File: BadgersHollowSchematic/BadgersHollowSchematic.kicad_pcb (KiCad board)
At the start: 2 copper layers, 33 x 48.3 mm, 5 parts

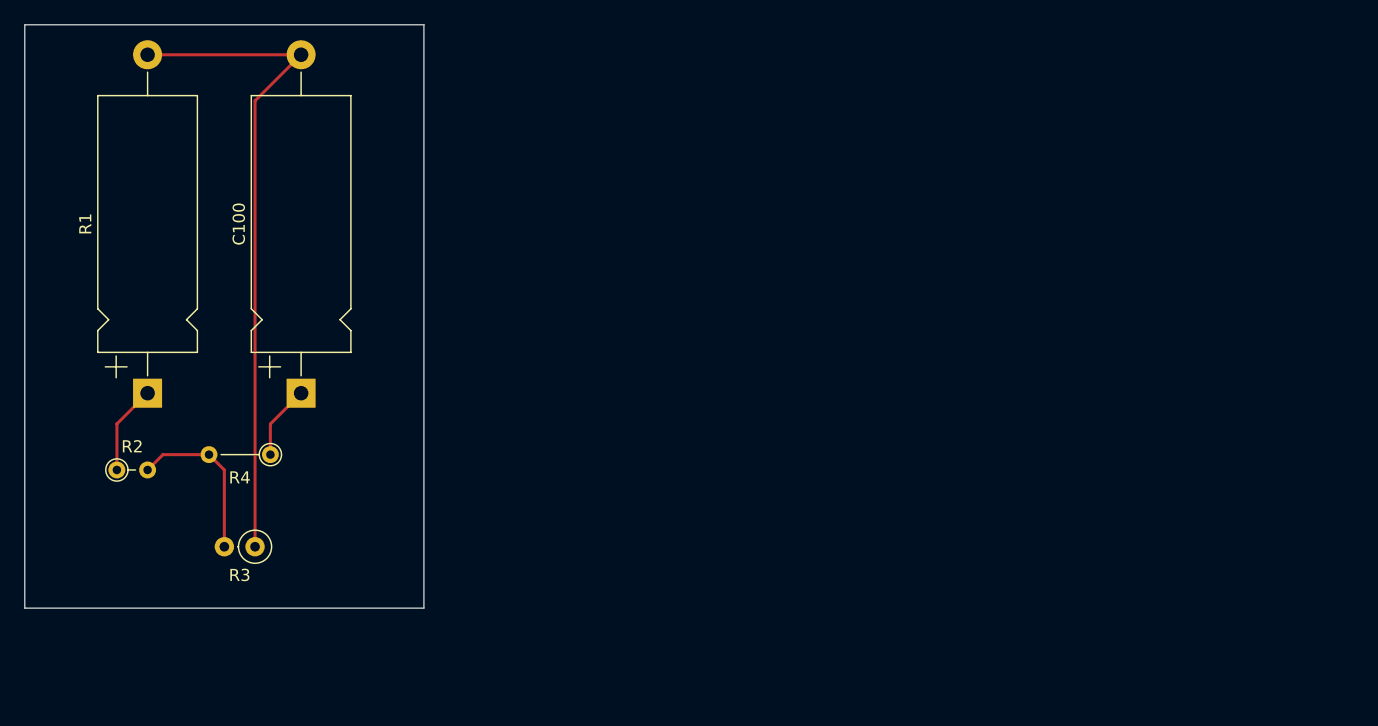
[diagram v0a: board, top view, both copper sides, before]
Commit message: Schematic down. Need to review, and map columns/rows to correct pins
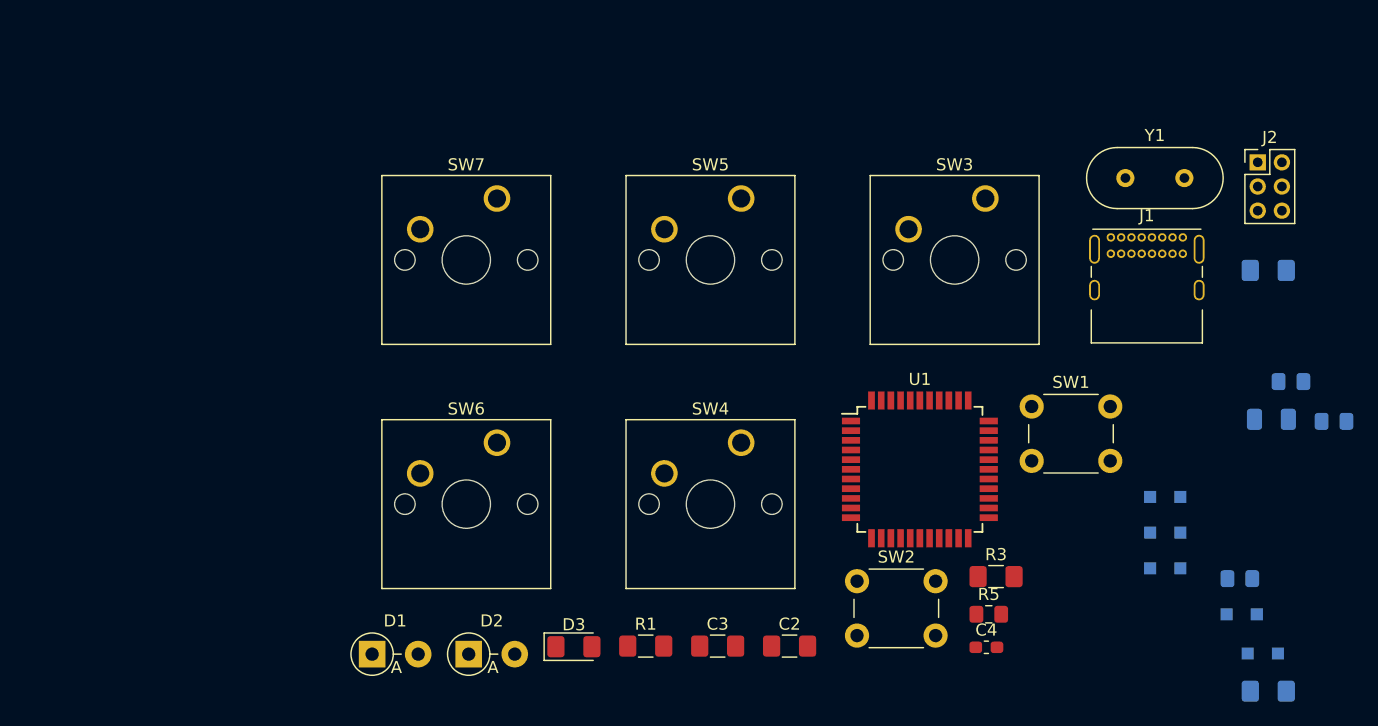
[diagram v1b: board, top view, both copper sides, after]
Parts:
- removed C100: 10, Capacitor_THT:CP_Axial_L21.0mm_D8.0mm_P28.00mm_Horizontal
- added C1: 22pF, Capacitor_SMD:C_1206_3216Metric_Pad1.42x1.75mm_HandSolder, B.Cu at (207.0, 71.1)
- added C2: 22pF, Capacitor_SMD:C_1206_3216Metric_Pad1.42x1.75mm_HandSolder, F.Cu at (167.4, 102.2)
- added C3: 1uF, Resistor_SMD:R_1206_3216Metric_Pad1.42x1.75mm_HandSolder, F.Cu at (161.5, 102.2)
- added C4: 10uF, Capacitor_SMD:C_0603_1608Metric_Pad1.05x0.95mm_HandSolder, F.Cu at (183.7, 102.3)
- added D1: 3.6V, Diode_THT:D_DO-41_SOD81_P3.81mm_Vertical_AnodeUp, F.Cu at (132.9, 102.9)
- added D2: 3.6V, Diode_THT:D_DO-41_SOD81_P3.81mm_Vertical_AnodeUp, F.Cu at (140.9, 102.9)
- added D3: LED, LED_SMD:LED_1206_3216Metric_Pad1.42x1.75mm_HandSolder, F.Cu at (149.6, 102.2)
- added D4: 1N4148, Diode_SMD:D_SOD-323_HandSoldering, B.Cu at (204.8, 99.6)
- added D5: 1N4148, Diode_SMD:D_SOD-323_HandSoldering, B.Cu at (198.5, 89.9)
- added D6: 1N4148, Diode_SMD:D_SOD-323_HandSoldering, B.Cu at (198.5, 92.8)
- added D7: 1N4148, Diode_SMD:D_SOD-323_HandSoldering, B.Cu at (206.6, 102.8)
- added D8: 1N4148, Diode_SMD:D_SOD-323_HandSoldering, B.Cu at (198.5, 95.8)
- added F1: Polyfuse_Small, Fuse:Fuse_1206_3216Metric, B.Cu at (207.3, 83.4)
- added J1: usbc_gct, Connector_USB:USB_C_Receptacle_GCT_USB4085, F.Cu at (194.0, 68.4)
- added J2: AVR-ISP-6, Connector_PinHeader_2.00mm:PinHeader_2x03_P2.00mm_Vertical, F.Cu at (206.1, 62.2)
- added R5: 22, Resistor_SMD:R_0805_2012Metric_Pad1.15x1.40mm_HandSolder, F.Cu at (183.9, 99.6)
- added R6: 1.5K, Resistor_SMD:R_0805_2012Metric_Pad1.15x1.40mm_HandSolder, B.Cu at (208.9, 80.3)
- added R7: 1.5K, Resistor_SMD:R_0805_2012Metric_Pad1.15x1.40mm_HandSolder, B.Cu at (204.7, 96.6)
- added SW1: SW_Push, Button_Switch_THT:SW_PUSH_6mm, F.Cu at (187.4, 82.4)
- added SW2: SW_Push, Button_Switch_THT:SW_PUSH_6mm, F.Cu at (173.0, 96.8)
- added SW3: SW_SPST, Button_Switch_Keyboard:SW_Cherry_MX_1.00u_PCB, F.Cu at (183.6, 65.2)
- added SW4: SW_SPST, Button_Switch_Keyboard:SW_Cherry_MX_1.00u_PCB, F.Cu at (163.4, 85.4)
- added SW5: SW_SPST, Button_Switch_Keyboard:SW_Cherry_MX_1.00u_PCB, F.Cu at (163.4, 65.2)
- added SW6: SW_SPST, Button_Switch_Keyboard:SW_Cherry_MX_1.00u_PCB, F.Cu at (143.2, 85.4)
- added SW7: SW_SPST, Button_Switch_Keyboard:SW_Cherry_MX_1.00u_PCB, F.Cu at (143.2, 65.2)
- added U1: ATmega32U4-AU, Package_QFP:TQFP-44_10x10mm_P0.8mm, F.Cu at (178.2, 87.6)
- added Y1: Crystal, Crystal:Crystal_HC49-U_Vertical, F.Cu at (195.2, 63.5)
- R1: value 100 -> 10K; footprint Capacitor_THT:CP_Axial_L21.0mm_D8.0mm_P28.00mm_Horizontal -> Resistor_SMD:R_1206_3216Metric_Pad1.42x1.75mm_HandSolder
- R2: value 200 -> 5.1K; footprint Resistor_THT:R_Axial_DIN0204_L3.6mm_D1.6mm_P2.54mm_Vertical -> Resistor_SMD:R_1206_3216Metric_Pad1.42x1.75mm_HandSolder; moved to B.Cu
- R3: value 300 -> 5.1K; footprint Resistor_THT:R_Axial_DIN0207_L6.3mm_D2.5mm_P2.54mm_Vertical -> Resistor_SMD:R_1206_3216Metric_Pad1.42x1.75mm_HandSolder
- R4: value 400 -> 22; footprint Resistor_THT:R_Axial_DIN0204_L3.6mm_D1.6mm_P5.08mm_Vertical -> Resistor_SMD:R_0805_2012Metric_Pad1.15x1.40mm_HandSolder; moved to B.Cu
- moved R2 97.0 mm to (207.0, 105.9)
- moved R4 88.0 mm to (212.4, 83.6), turned to 0 degrees
- moved R3 61.3 mm to (184.5, 96.5), turned to 0 degrees
- moved R1 46.2 mm to (155.5, 102.2), turned to 0 degrees
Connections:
- R1 pad 1: Net-(R1-Pad1) -> +5V
- R1 pad 2: Net-(C100-Pad2) -> Reset
- R2 pad 1: Net-(R1-Pad1) -> GND
- R2 pad 2: GND -> Net-(J1-PadA5)
- R3 pad 1: Net-(C100-Pad2) -> GND
- R3 pad 2: GND -> Net-(J1-PadB5)
- R4 pad 1: Net-(C100-Pad1) -> d-
- R4 pad 2: GND -> Net-(D1-Pad1)
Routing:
- net Net-(C100-Pad2): track 55.0 -> 0.00 mm
- net GND: track 13.8 -> 0.00 mm
- net Net-(R1-Pad1): track 7.40 -> 0.00 mm
- net Net-(C100-Pad1): track 6.13 -> 0.00 mm
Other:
- board outline removed

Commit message: Working on layout
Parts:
- added C10: 0.1uF, Capacitor_SMD:C_0805_2012Metric_Pad1.15x1.40mm_HandSolder, B.Cu at (230.5, 64.8)
- added C11: 0.1uF, Capacitor_SMD:C_0805_2012Metric_Pad1.15x1.40mm_HandSolder, B.Cu at (241.3, 73.7)
- added C12: 0.1uF, Capacitor_SMD:C_0805_2012Metric_Pad1.15x1.40mm_HandSolder, B.Cu at (241.3, 68.6)
- added C13: 0.1uF, Capacitor_SMD:C_0805_2012Metric_Pad1.15x1.40mm_HandSolder, B.Cu at (227.1, 57.8)
- added C14: 0.1uF, Capacitor_SMD:C_0805_2012Metric_Pad1.15x1.40mm_HandSolder, B.Cu at (233.0, 59.1)
- added C15: 0.1uF, Capacitor_SMD:C_0805_2012Metric_Pad1.15x1.40mm_HandSolder, B.Cu at (204.5, 81.3)
- added C16: 0.1uF, Capacitor_SMD:C_0805_2012Metric_Pad1.15x1.40mm_HandSolder, B.Cu at (233.3, 73.7)
- added C17: 0.1uF, Capacitor_SMD:C_0805_2012Metric_Pad1.15x1.40mm_HandSolder, B.Cu at (237.5, 78.7)
- added C18: 0.1uF, Capacitor_SMD:C_0805_2012Metric_Pad1.15x1.40mm_HandSolder, B.Cu at (203.2, 74.9)
- added C19: 0.1uF, Capacitor_SMD:C_0805_2012Metric_Pad1.15x1.40mm_HandSolder, B.Cu at (224.3, 78.1)
- added C20: 0.1uF, Capacitor_SMD:C_0805_2012Metric_Pad1.15x1.40mm_HandSolder, B.Cu at (224.5, 65.9)
- added C21: 0.1uF, Capacitor_SMD:C_0805_2012Metric_Pad1.15x1.40mm_HandSolder, B.Cu at (201.8, 69.1)
- added C22: 0.1uF, Capacitor_SMD:C_0805_2012Metric_Pad1.15x1.40mm_HandSolder, B.Cu at (227.0, 68.9)
- added C23: 0.1uF, Capacitor_SMD:C_0805_2012Metric_Pad1.15x1.40mm_HandSolder, B.Cu at (218.2, 72.6)
- added C24: 0.1uF, Capacitor_SMD:C_0805_2012Metric_Pad1.15x1.40mm_HandSolder, B.Cu at (216.0, 61.4)
- added C25: 0.1uF, Capacitor_SMD:C_0805_2012Metric_Pad1.15x1.40mm_HandSolder, B.Cu at (206.8, 69.5)
- added C26: 0.1uF, Capacitor_SMD:C_0805_2012Metric_Pad1.15x1.40mm_HandSolder, B.Cu at (212.7, 73.7)
- added C27: 0.1uF, Capacitor_SMD:C_0805_2012Metric_Pad1.15x1.40mm_HandSolder, B.Cu at (216.5, 78.7)
- added C28: 0.1uF, Capacitor_SMD:C_0805_2012Metric_Pad1.15x1.40mm_HandSolder, B.Cu at (221.0, 61.8)
- added C5: 0.1uF, Capacitor_SMD:C_0805_2012Metric_Pad1.15x1.40mm_HandSolder, B.Cu at (231.8, 68.9)
- added C6: 0.1uF, Capacitor_SMD:C_0805_2012Metric_Pad1.15x1.40mm_HandSolder, B.Cu at (226.1, 73.0)
- added C7: 0.1uF, Capacitor_SMD:C_0805_2012Metric_Pad1.15x1.40mm_HandSolder, B.Cu at (218.2, 69.6)
- added C8: 0.1uF, Capacitor_SMD:C_0805_2012Metric_Pad1.15x1.40mm_HandSolder, B.Cu at (229.1, 78.1)
- added C9: 0.1uF, Capacitor_SMD:C_0805_2012Metric_Pad1.15x1.40mm_HandSolder, B.Cu at (234.9, 63.5)
- added D10: 1N4148, Diode_SMD:D_SOD-323_HandSoldering, F.Cu at (244.8, 105.2)
- added D11: 1N4148, Diode_SMD:D_SOD-323_HandSoldering, F.Cu at (219.7, 130.0)
- added D12: 1N4148, Diode_SMD:D_SOD-323_HandSoldering, F.Cu at (262.8, 109.2)
- added D13: 1N4148, Diode_SMD:D_SOD-323_HandSoldering, F.Cu at (247.3, 101.9)
- added D14: 1N4148, Diode_SMD:D_SOD-323_HandSoldering, F.Cu at (278.8, 94.0)
- added D15: 1N4148, Diode_SMD:D_SOD-323_HandSoldering, F.Cu at (273.7, 94.0)
- added D16: 1N4148, Diode_SMD:D_SOD-323_HandSoldering, F.Cu at (253.5, 114.6)
- added D18: 1N4148, Diode_SMD:D_SOD-323_HandSoldering, F.Cu at (250.1, 121.2)
- added D19: 1N4148, Diode_SMD:D_SOD-323_HandSoldering, F.Cu at (238.9, 111.4)
- added D20: 1N4148, Diode_SMD:D_SOD-323_HandSoldering, F.Cu at (238.9, 108.5)
- added D21: 1N4148, Diode_SMD:D_SOD-323_HandSoldering, F.Cu at (242.6, 127.8)
- added D22: 1N4148, Diode_SMD:D_SOD-323_HandSoldering, F.Cu at (273.7, 97.0)
- added D23: 1N4148, Diode_SMD:D_SOD-323_HandSoldering, F.Cu at (265.3, 105.5)
- added D24: 1N4148, Diode_SMD:D_SOD-323_HandSoldering, F.Cu at (245.1, 124.2)
- added D25: 1N4148, Diode_SMD:D_SOD-323_HandSoldering, F.Cu at (253.5, 117.5)
- added D26: 1N4148, Diode_SMD:D_SOD-323_HandSoldering, F.Cu at (230.4, 118.4)
- added D27: 1N4148, Diode_SMD:D_SOD-323_HandSoldering, F.Cu at (249.7, 86.4)
- added D28: 1N4148, Diode_SMD:D_SOD-323_HandSoldering, F.Cu at (265.3, 102.6)
- added D29: SK6812, LED_SMD:LED_SK6812_PLCC4_5.0x5.0mm_P3.2mm, B.Cu at (194.1, 36.3)
- added D30: SK6812, LED_SMD:LED_SK6812_PLCC4_5.0x5.0mm_P3.2mm, B.Cu at (181.5, 19.8)
- added D31: SK6812, LED_SMD:LED_SK6812_PLCC4_5.0x5.0mm_P3.2mm, B.Cu at (189.9, 26.4)
- added D32: SK6812, LED_SMD:LED_SK6812_PLCC4_5.0x5.0mm_P3.2mm, B.Cu at (212.1, 41.9)
- added D33: SK6812, LED_SMD:LED_SK6812_PLCC4_5.0x5.0mm_P3.2mm, B.Cu at (222.4, 50.4)
- added D34: SK6812, LED_SMD:LED_SK6812_PLCC4_5.0x5.0mm_P3.2mm, B.Cu at (230.8, 43.8)
- added D35: SK6812, LED_SMD:LED_SK6812_PLCC4_5.0x5.0mm_P3.2mm, B.Cu at (173.0, 24.5)
- added D36: SK6812, LED_SMD:LED_SK6812_PLCC4_5.0x5.0mm_P3.2mm, B.Cu at (189.7, 10.2)
- added D37: SK6812, LED_SMD:LED_SK6812_PLCC4_5.0x5.0mm_P3.2mm, B.Cu at (196.0, 53.3)
- added D38: SK6812, LED_SMD:LED_SK6812_PLCC4_5.0x5.0mm_P3.2mm, B.Cu at (201.7, 22.4)
- added D39: SK6812, LED_SMD:LED_SK6812_PLCC4_5.0x5.0mm_P3.2mm, B.Cu at (210.1, 29.1)
- added D40: SK6812, LED_SMD:LED_SK6812_PLCC4_5.0x5.0mm_P3.2mm, B.Cu at (209.6, 15.2)
- added D41: SK6812, LED_SMD:LED_SK6812_PLCC4_5.0x5.0mm_P3.2mm, B.Cu at (185.7, 36.3)
- added D42: SK6812, LED_SMD:LED_SK6812_PLCC4_5.0x5.0mm_P3.2mm, B.Cu at (198.1, 10.2)
- added D43: SK6812, LED_SMD:LED_SK6812_PLCC4_5.0x5.0mm_P3.2mm, B.Cu at (181.5, 26.4)
- added D44: SK6812, LED_SMD:LED_SK6812_PLCC4_5.0x5.0mm_P3.2mm, B.Cu at (173.0, 17.9)
- added D45: SK6812, LED_SMD:LED_SK6812_PLCC4_5.0x5.0mm_P3.2mm, B.Cu at (210.2, 48.3)
- added D46: SK6812, LED_SMD:LED_SK6812_PLCC4_5.0x5.0mm_P3.2mm, B.Cu at (179.3, 11.2)
- added D47: SK6812, LED_SMD:LED_SK6812_PLCC4_5.0x5.0mm_P3.2mm, B.Cu at (189.9, 19.8)
- added D48: SK6812, LED_SMD:LED_SK6812_PLCC4_5.0x5.0mm_P3.2mm, B.Cu at (196.0, 46.7)
- added D49: SK6812, LED_SMD:LED_SK6812_PLCC4_5.0x5.0mm_P3.2mm, B.Cu at (210.1, 22.4)
- added D50: SK6812, LED_SMD:LED_SK6812_PLCC4_5.0x5.0mm_P3.2mm, B.Cu at (230.8, 50.4)
- added D51: SK6812, LED_SMD:LED_SK6812_PLCC4_5.0x5.0mm_P3.2mm, B.Cu at (222.4, 43.8)
- added D52: SK6812, LED_SMD:LED_SK6812_PLCC4_5.0x5.0mm_P3.2mm, B.Cu at (170.9, 11.2)
- added D9: 1N4148, Diode_SMD:D_SOD-323_HandSoldering, F.Cu at (221.7, 126.8)
- added SW10: SW_SPST, Button_Switch_Keyboard:SW_Cherry_MX_1.00u_PCB, F.Cu at (85.7, 73.0)
- added SW11: SW_SPST, Button_Switch_Keyboard:SW_Cherry_MX_2.00u_Vertical_PCB, F.Cu at (104.8, 82.5)
- added SW12: SW_SPST, Button_Switch_Keyboard:SW_Cherry_MX_1.00u_PCB, F.Cu at (123.8, 73.0)
- added SW13: SW_SPST, Button_Switch_Keyboard:SW_Cherry_MX_1.00u_PCB, F.Cu at (47.6, 92.1)
- added SW14: SW_SPST, Button_Switch_Keyboard:SW_Cherry_MX_1.00u_PCB, F.Cu at (66.7, 92.1)
- added SW15: SW_SPST, Button_Switch_Keyboard:SW_Cherry_MX_1.00u_PCB, F.Cu at (85.7, 92.1)
- added SW17: SW_SPST, Button_Switch_Keyboard:SW_Cherry_MX_1.00u_PCB, F.Cu at (123.8, 92.1)
- added SW18: SW_SPST, Button_Switch_Keyboard:SW_Cherry_MX_1.00u_PCB, F.Cu at (47.6, 111.1)
- added SW19: SW_SPST, Button_Switch_Keyboard:SW_Cherry_MX_1.00u_PCB, F.Cu at (66.7, 111.1)
- added SW20: SW_SPST, Button_Switch_Keyboard:SW_Cherry_MX_1.00u_PCB, F.Cu at (85.7, 111.1)
- added SW21: SW_SPST, Button_Switch_Keyboard:SW_Cherry_MX_2.00u_Vertical_PCB, F.Cu at (104.8, 120.7)
- added SW22: SW_SPST, Button_Switch_Keyboard:SW_Cherry_MX_1.00u_PCB, F.Cu at (123.8, 111.1)
- added SW23: SW_SPST, Button_Switch_Keyboard:SW_Cherry_MX_1.00u_PCB, F.Cu at (47.6, 130.2)
- added SW24: SW_SPST, Button_Switch_Keyboard:SW_Cherry_MX_1.00u_PCB, F.Cu at (66.7, 130.2)
- added SW25: SW_SPST, Button_Switch_Keyboard:SW_Cherry_MX_1.00u_PCB, F.Cu at (85.7, 130.2)
- added SW26: SW_SPST, Button_Switch_Keyboard:SW_Cherry_MX_1.00u_PCB, F.Cu at (123.8, 130.2)
- added SW27: Rotory Encoder, Rotary_Encoder:RotaryEncoder_Alps_EC11E-Switch_Vertical_H20mm_CircularMountingHoles, F.Cu at (109.9, 41.9)
- added SW8: SW_SPST, Button_Switch_Keyboard:SW_Cherry_MX_1.00u_PCB, F.Cu at (47.6, 73.0)
- added SW9: SW_SPST, Button_Switch_Keyboard:SW_Cherry_MX_1.00u_PCB, F.Cu at (66.7, 73.0)
- C1, D4, D5, D6, D7, D8, F1, R2, R4, R6, R7: moved to F.Cu
- D3: value LED -> PWR LED
- J2, SW1, SW2: moved to B.Cu
- moved C1 172.7 mm to (38.6, 33.0)
- moved R4 166.3 mm to (53.8, 33.5), turned to 90 degrees
- moved F1 158.3 mm to (57.4, 32.5)
- moved Y1 157.5 mm to (38.7, 45.6), turned to 90 degrees
- moved R5 147.7 mm to (51.8, 33.5), turned to 270 degrees
- moved C2 145.0 mm to (38.6, 35.6)
- moved R7 144.4 mm to (73.2, 37.1), turned to 180 degrees
- moved SW3 136.4 mm to (47.6, 54.0)
- moved U1 135.3 mm to (50.8, 42.0), turned to 270 degrees
- moved J1 129.2 mm to (67.9, 40.1), turned to 180 degrees
- moved D3 102.1 mm to (73.7, 34.0), turned to 180 degrees
- moved SW4 101.7 mm to (66.7, 54.0)
- moved D2 97.6 mm to (63.5, 43.3)
- moved J2 90.6 mm to (116.8, 47.0)
- moved D1 89.4 mm to (63.5, 46.5)
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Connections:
- D4 pad 1: Net-(D4-Pad1) -> row0
- D5 pad 1: Net-(D5-Pad1) -> row0
- D6 pad 1: Net-(D6-Pad1) -> row0
- D7 pad 1: Net-(D7-Pad1) -> row0
- D8 pad 1: Net-(D8-Pad1) -> row0
- SW3 pad 2: Net-(SW3-Pad2) -> col0
- SW4 pad 2: Net-(SW4-Pad2) -> col1
- SW5 pad 2: Net-(SW5-Pad2) -> col2
- SW6 pad 2: Net-(SW6-Pad2) -> col3
- SW7 pad 2: Net-(SW7-Pad2) -> col4
- U1 pad 10: Net-(U1-Pad10) -> MOSI
- U1 pad 11: Net-(U1-Pad11) -> MISO
- U1 pad 18: Net-(U1-Pad18) -> col0
- U1 pad 19: Net-(U1-Pad19) -> col1
- U1 pad 20: Net-(U1-Pad20) -> col2
- U1 pad 21: Net-(U1-Pad21) -> col3
- U1 pad 25: boot -> col4
- U1 pad 28: Net-(U1-Pad28) -> LEDIN
- U1 pad 29: Net-(U1-Pad29) -> rencb
- U1 pad 30: Net-(U1-Pad30) -> renca
- U1 pad 33: Net-(U1-Pad33) -> boot
- U1 pad 37: Net-(U1-Pad37) -> row0
- U1 pad 38: Net-(U1-Pad38) -> row1
- U1 pad 39: Net-(U1-Pad39) -> row2
- U1 pad 40: Net-(U1-Pad40) -> row3
- U1 pad 41: Net-(U1-Pad41) -> rer
- U1 pad 9: Net-(U1-Pad9) -> SCK
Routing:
- net Net-(C2-Pad1): track 0.00 -> 10.7 mm
- net Net-(C1-Pad1): track 0.00 -> 8.36 mm
- net GND: track 0.00 -> 2.54 mm
- net d-: track 0.00 -> 2.05 mm
- net d+: track 0.00 -> 2.03 mm
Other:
- copper layers 2 -> 4

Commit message: Layout done. Now working on routing
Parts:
- removed C10, C13, C16, C19, C22, C25, C28: 0.1uF, Capacitor_SMD:C_0805_2012Metric_Pad1.15x1.40mm_HandSolder
- removed D46, D47, D48, D49, D50, D51, D52: SK6812, LED_SMD:LED_SK6812_PLCC4_5.0x5.0mm_P3.2mm
- added REF**: MountingHole_3.2mm_M3, MountingHole:MountingHole_3.2mm_M3, F.Cu at (33.0, 39.9)
- added REF**: MountingHole_3.2mm_M3, MountingHole:MountingHole_3.2mm_M3, F.Cu at (54.6, 72.4)
- added REF**: MountingHole_3.2mm_M3, MountingHole:MountingHole_3.2mm_M3, F.Cu at (102.1, 72.4)
- added REF**: MountingHole_3.2mm_M3, MountingHole:MountingHole_3.2mm_M3, F.Cu at (33.8, 139.7)
- added REF**: MountingHole_3.2mm_M3, MountingHole:MountingHole_3.2mm_M3, F.Cu at (54.6, 139.2)
- added REF**: MountingHole_3.2mm_M3, MountingHole:MountingHole_3.2mm_M3, F.Cu at (101.9, 139.2)
- added REF**: MountingHole_3.2mm_M3, MountingHole:MountingHole_3.2mm_M3, F.Cu at (131.8, 139.7)
- added REF**: MountingHole_3.2mm_M3, MountingHole:MountingHole_3.2mm_M3, F.Cu at (133.3, 40.1)
- C4, D10, D11, D12, D13, D14, D15, D16, D18, D19, D20, D21, D22, D23, D24, D25, D26, D27, D28, D4, D5, D6, D7, D8, D9, F1, R1: moved to B.Cu
- moved D14 233.7 mm to (45.2, 102.6)
- moved C3 215.8 mm to (46.7, 33.0)
- moved D15 209.9 mm to (64.0, 102.6)
- moved D34 208.7 mm to (39.1, 126.2)
- moved D24 200.6 mm to (45.2, 140.7)
- moved D5 200.2 mm to (64.2, 64.5)
- moved C11 197.7 mm to (43.7, 68.8), turned to 270 degrees
- moved C17 195.9 mm to (43.7, 107.2), turned to 270 degrees
- moved D19 193.9 mm to (45.2, 121.9)
- moved D6 193.7 mm to (83.3, 64.5)
- moved D33 191.9 mm to (39.1, 107.2)
- moved D4 191.6 mm to (45.2, 64.5)
- moved C14 191.6 mm to (43.7, 88.1), turned to 270 degrees
- moved C5 191.4 mm to (43.4, 34.5), turned to 270 degrees
- moved D25 190.7 mm to (64.2, 140.7)
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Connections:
- D45 pad 4: Net-(D45-Pad4) -> GND
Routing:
- net Reset: track 0.00 -> 104.9 mm, vias 0 -> 2
- net col3: track 0.00 -> 87.6 mm
- net col2: track 0.00 -> 76.2 mm
- net col4: track 0.00 -> 76.2 mm
- net col1: track 0.00 -> 76.2 mm
- net col0: track 0.00 -> 76.2 mm
- net boot: track 0.00 -> 74.2 mm
- net +5V: track 0.00 -> 53.1 mm, vias 0 -> 1
- net Net-(C11-Pad1): track 0.00 -> 39.2 mm
- net Net-(D1-Pad1): track 0.00 -> 26.0 mm
- net Net-(D2-Pad1): track 0.00 -> 22.8 mm
- net VCC: track 0.00 -> 17.2 mm, vias 0 -> 1
- net Net-(D12-Pad2): track 0.00 -> 11.5 mm
- net Net-(D22-Pad2): track 0.00 -> 11.5 mm
- net Net-(D20-Pad2): track 0.00 -> 11.4 mm
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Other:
- board outline added: 108.2 x 119.1 mm
- copper layers 4 -> 2

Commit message: First rev of the board, with gbr files
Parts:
- removed the REF** at (33.0, 39.9)
- removed the REF** at (54.6, 72.4)
- removed the REF** at (54.6, 139.2)
- added REF**: MountingHole_3.2mm_M3, MountingHole:MountingHole_3.2mm_M3, F.Cu at (32.4, 39.8)
- C1, C2, R2, R3: moved to B.Cu
- C4, F1, J2, SW1, SW2: moved to F.Cu
- moved J2 54.4 mm to (64.8, 42.4), turned to 270 degrees
- moved C1 47.7 mm to (86.3, 34.3), turned to 90 degrees
- moved Y1 46.2 mm to (84.8, 41.2), turned to 270 degrees
- moved C2 45.1 mm to (83.7, 34.3), turned to 90 degrees
- moved R2 40.2 mm to (40.7, 41.3)
- moved R3 39.4 mm to (40.8, 38.8)
- moved D3 32.8 mm to (40.9, 31.7)
- moved R7 32.2 mm to (41.0, 36.1)
- moved C4 27.2 mm to (45.6, 43.3), turned to 90 degrees
- moved U1 22.9 mm to (73.2, 37.4), turned to 0 degrees
- moved R6 20.7 mm to (50.1, 42.2), turned to 90 degrees
- moved C3 18.0 mm to (63.6, 39.2), turned to 180 degrees
- moved J1 15.0 mm to (53.0, 39.1)
- moved F1 14.0 mm to (47.9, 42.7), turned to 90 degrees
- moved D1 12.7 mm to (56.9, 35.2), turned to 90 degrees
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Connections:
- C11 pad 1: Net-(C11-Pad1) -> +5V
- C12 pad 1: Net-(C11-Pad1) -> +5V
- C14 pad 1: Net-(C11-Pad1) -> +5V
- C15 pad 1: Net-(C11-Pad1) -> +5V
- C17 pad 1: Net-(C11-Pad1) -> +5V
- C18 pad 1: Net-(C11-Pad1) -> +5V
- C20 pad 1: Net-(C11-Pad1) -> +5V
- C21 pad 1: Net-(C11-Pad1) -> +5V
- C23 pad 1: Net-(C11-Pad1) -> +5V
- C24 pad 1: Net-(C11-Pad1) -> +5V
- C26 pad 1: Net-(C11-Pad1) -> +5V
- C27 pad 1: Net-(C11-Pad1) -> +5V
- C5 pad 1: Net-(C11-Pad1) -> +5V
- C6 pad 1: Net-(C11-Pad1) -> +5V
- C7 pad 1: Net-(C11-Pad1) -> +5V
- C8 pad 1: Net-(C11-Pad1) -> +5V
- C9 pad 1: Net-(C11-Pad1) -> +5V
- D29 pad 3: Net-(C11-Pad1) -> +5V
- D30 pad 3: Net-(C11-Pad1) -> +5V
- D31 pad 3: Net-(C11-Pad1) -> +5V
- D32 pad 3: Net-(C11-Pad1) -> +5V
- D33 pad 2: Net-(D33-Pad2) -> Net-(D32-Pad4)
- D33 pad 3: Net-(C11-Pad1) -> +5V
- D34 pad 3: Net-(C11-Pad1) -> +5V
- D35 pad 3: Net-(C11-Pad1) -> +5V
- D36 pad 3: Net-(C11-Pad1) -> +5V
- D37 pad 3: Net-(C11-Pad1) -> +5V
- D38 pad 3: Net-(C11-Pad1) -> +5V
- D39 pad 3: Net-(C11-Pad1) -> +5V
- D40 pad 3: Net-(C11-Pad1) -> +5V
- D41 pad 2: Net-(D41-Pad2) -> Net-(D40-Pad4)
- D41 pad 3: Net-(C11-Pad1) -> +5V
- D42 pad 3: Net-(C11-Pad1) -> +5V
- D43 pad 3: Net-(C11-Pad1) -> +5V
- D44 pad 3: Net-(C11-Pad1) -> +5V
- D45 pad 3: Net-(C11-Pad1) -> +5V
- U1 pad 22: Net-(U1-Pad22) -> col4
- U1 pad 25: col4 -> Net-(U1-Pad25)
- U1 pad 37: row0 -> row1
- U1 pad 38: row1 -> row2
- U1 pad 39: row2 -> row3
- U1 pad 40: row3 -> rer
- U1 pad 41: rer -> row0
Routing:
- net GND: track 2.54 -> 607.6 mm, vias 0 -> 27
- net +5V: track 53.1 -> 479.9 mm, vias 1 -> 4
- net rer: track 0.00 -> 212.5 mm, vias 0 -> 4
- net row3: track 0.00 -> 180.1 mm, vias 0 -> 3
- net row2: track 0.00 -> 153.6 mm, vias 0 -> 3
- net row1: track 0.00 -> 142.7 mm, vias 0 -> 3
- net row0: track 0.00 -> 115.5 mm, vias 0 -> 3
- net LEDIN: track 0.00 -> 60.9 mm, vias 0 -> 1
- net col4: track 76.2 -> 122.0 mm
- net Net-(C11-Pad1): track 39.2 -> 0.00 mm
- net col0: track 76.2 -> 115.1 mm
- net rencb: track 0.00 -> 37.5 mm, vias 0 -> 1
- net renca: track 0.00 -> 37.0 mm, vias 0 -> 2
- net Net-(D39-Pad4): track 0.00 -> 30.9 mm
- net col3: track 87.6 -> 118.1 mm
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- added copper zone on B.Cu, net GND
- added copper zone on F.Cu, net GND
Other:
- net class Default: clearance 0.2 -> 0.15
- rule trace_clearance: 0.2 -> 0.15
- board text added: "Badgers Hollow V1 Designed By: Spencer Lombardo"
